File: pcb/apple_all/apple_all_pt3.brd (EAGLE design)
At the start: 56 x 65 mm, 49 parts, among them IC1 STM32F072C8T6, SW1 324_SW, SW2 324_SW, SW3 324_SW

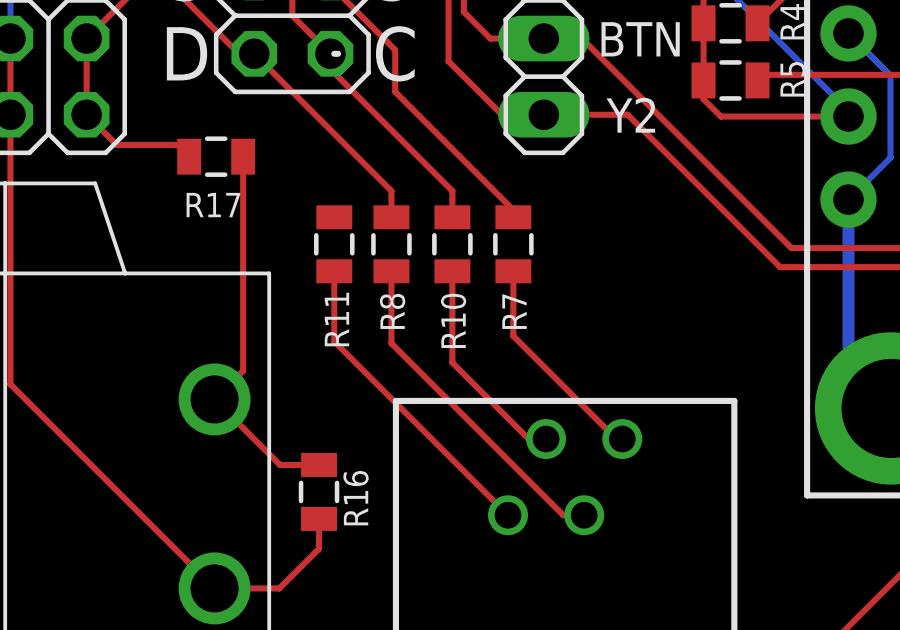
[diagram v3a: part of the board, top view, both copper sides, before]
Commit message: m0110 keyboard working, added busy signal and protocol switching
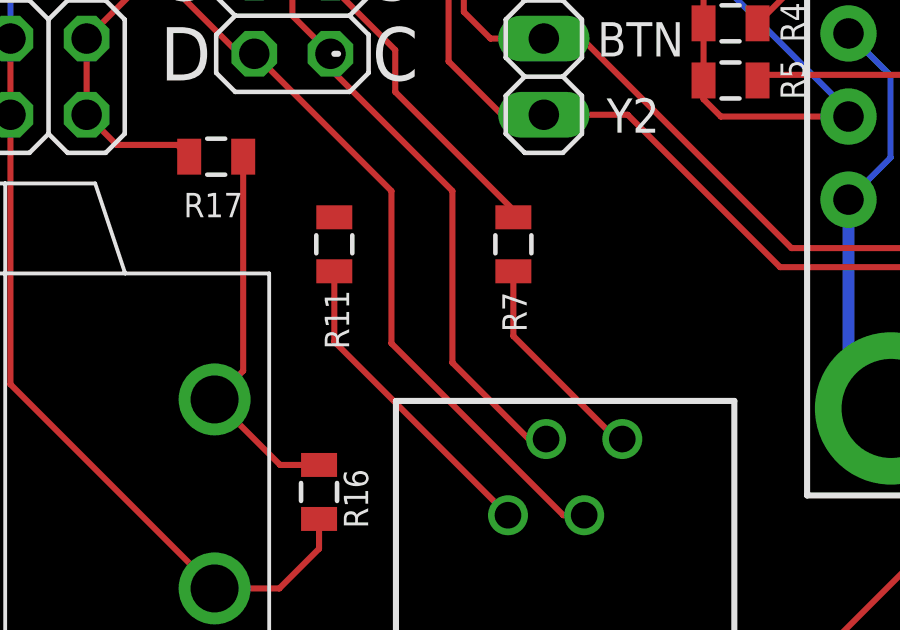
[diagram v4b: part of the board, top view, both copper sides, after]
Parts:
- removed R10, R8: 200, SparkFun-Passives:0805
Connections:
- removed net N$10: R8.2, U$8.3
- removed net N$20: R10.2, U$8.2
- net N$19: now also U$8.2; no longer R10.1
- net N$25: now also U$8.3; no longer R8.1
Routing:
- net N$25: track 14.9 -> 27.9 mm
- net N$10: track 11.2 -> 0.00 mm
- net N$19: track 16.5 -> 25.6 mm
- net N$20: track 7.22 -> 0.00 mm
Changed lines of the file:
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@@
 <layer number="19" name="Unrouted" color="6" fill="1" visible="yes" active="yes"/>
 <layer number="20" name="Dimension" color="24" fill="1" visible="yes" active="yes"/>
-<layer number="21" name="tPlace" color="7" fill="1" visible="yes" active="yes"/>
-<layer number="22" name="bPlace" color="7" fill="1" visible="yes" active="yes"/>
+<layer number="21" name="tPlace" color="7" fill="1" visible="no" active="yes"/>
+<layer number="22" name="bPlace" color="7" fill="1" visible="no" active="yes"/>
 <layer number="23" name="tOrigins" color="15" fill="1" visible="yes" active="yes"/>
 <layer number="24" name="bOrigins" color="15" fill="1" visible="yes" active="yes"/>
-<layer number="25" name="tNames" color="7" fill="1" visible="yes" active="yes"/>
-<layer number="26" name="bNames" color="7" fill="1" visible="yes" active="yes"/>
-<layer number="27" name="tValues" color="7" fill="1" visible="yes" active="yes"/>
-<layer number="28" name="bValues" color="7" fill="1" visible="yes" active="yes"/>
+<layer number="25" name="tNames" color="7" fill="1" visible="no" active="yes"/>
+<layer number="26" name="bNames" color="7" fill="1" visible="no" active="yes"/>
+<layer number="27" name="tValues" color="7" fill="1" visible="no" active="yes"/>
+<layer number="28" name="bValues" color="7" fill="1" visible="no" active="yes"/>
 <layer number="29" name="tStop" color="7" fill="3" visible="no" active="yes"/>
 <layer number="30" name="bStop" color="7" fill="6" visible="no" active="yes"/>
@@
 <layer number="49" name="Reference" color="7" fill="1" visible="no" active="yes"/>
 <layer number="50" name="dxf" color="7" fill="1" visible="no" active="no"/>
-<layer number="51" name="tDocu" color="7" fill="1" visible="yes" active="yes"/>
-<layer number="52" name="bDocu" color="7" fill="1" visible="yes" active="yes"/>
+<layer number="51" name="tDocu" color="7" fill="1" visible="no" active="yes"/>
+<layer number="52" name="bDocu" color="7" fill="1" visible="no" active="yes"/>
 <layer number="53" name="tGND_GNDA" color="7" fill="1" visible="no" active="no"/>
 <layer number="54" name="bGND_GNDA" color="7" fill="1" visible="no" active="no"/>
@@
 <attribute name="NAME" x="34.3535" y="19.05" size="0.8128" layer="25" rot="R90"/>
 </element>
-<element name="R8" library="SparkFun-Passives" package="0805" value="200" x="29.845" y="21.971" smashed="yes" rot="R270">
-<attribute name="NAME" x="30.2895" y="19.05" size="0.8128" layer="25" rot="R90"/>
-</element>
-<element name="R10" library="SparkFun-Passives" package="0805" value="200" x="31.877" y="21.971" smashed="yes" rot="R270">
-<attribute name="NAME" x="32.3215" y="18.415" size="0.8128" layer="25" rot="R90"/>
-</element>
 <element name="R11" library="SparkFun-Passives" package="0805" value="200" x="27.94" y="21.971" smashed="yes" rot="R270">
 <attribute name="NAME" x="27.6225" y="20.447" size="0.8128" layer="25" rot="R270"/>
@@
 <wire x1="37.54" y1="15.48" x2="37.341" y2="15.48" width="0.2032" layer="1"/>
 </signal>
-<signal name="N$10">
-<contactref element="U$8" pad="3"/>
-<contactref element="R8" pad="2"/>
-<wire x1="29.845" y1="21.071" x2="29.845" y2="18.669" width="0.2032" layer="1"/>
-<wire x1="35.574" y1="12.94" x2="36.27" y2="12.94" width="0.2032" layer="1"/>
-<wire x1="29.845" y1="18.669" x2="35.574" y2="12.94" width="0.2032" layer="1"/>
-</signal>
-<signal name="N$20">
-<contactref element="U$8" pad="2"/>
-<contactref element="R10" pad="2"/>
-<wire x1="34.42" y1="15.48" x2="31.877" y2="18.023" width="0.2032" layer="1"/>
-<wire x1="31.877" y1="21.071" x2="31.877" y2="18.023" width="0.2032" layer="1"/>
-<wire x1="34.42" y1="15.48" x2="35" y2="15.48" width="0.2032" layer="1"/>
-</signal>
 <signal name="N$21">
 <contactref element="U$8" pad="1"/>
@@
 <contactref element="JP3" pad="4"/>
 <contactref element="IC1" pad="21"/>
-<contactref element="R10" pad="1"/>
-<wire x1="27.813" y1="27.813" x2="31.877" y2="23.749" width="0.2032" layer="1"/>
 <wire x1="27.813" y1="28.321" x2="27.813" y2="27.813" width="0.2032" layer="1"/>
-<wire x1="31.877" y1="23.749" x2="31.877" y2="22.871" width="0.2032" layer="1"/>
 <wire x1="27.813" y1="28.321" x2="26.543" y2="29.591" width="0.2032" layer="1"/>
 <wire x1="26.543" y1="31.75" x2="26.035" y2="32.258" width="0.2032" layer="1"/>
@@
 <wire x1="26.543" y1="29.591" x2="26.543" y2="31.75" width="0.2032" layer="1"/>
 <wire x1="23.749" y1="32.258" x2="23.25" y2="32.757" width="0.2032" layer="1"/>
+<contactref element="U$8" pad="2"/>
+<wire x1="31.877" y1="18.023" x2="34.42" y2="15.48" width="0.2032" layer="1"/>
+<wire x1="34.42" y1="15.48" x2="35" y2="15.48" width="0.2032" layer="1"/>
+<wire x1="27.813" y1="27.813" x2="31.877" y2="23.749" width="0.2032" layer="1"/>
+<wire x1="31.877" y1="23.749" x2="31.877" y2="18.023" width="0.2032" layer="1"/>
 </signal>
 <signal name="N$25">
-<contactref element="R8" pad="1"/>
 <contactref element="JP3" pad="3"/>
 <contactref element="IC1" pad="20"/>
-<wire x1="25.273" y1="28.321" x2="29.845" y2="23.749" width="0.2032" layer="1"/>
-<wire x1="29.845" y1="23.749" x2="29.845" y2="22.871" width="0.2032" layer="1"/>
 <wire x1="22.75" y1="34.5" x2="22.75" y2="30.336" width="0.2032" layer="1"/>
 <wire x1="24.765" y1="28.321" x2="25.273" y2="28.321" width="0.2032" layer="1"/>
 <wire x1="22.75" y1="30.336" x2="24.765" y2="28.321" width="0.2032" layer="1"/>
+<contactref element="U$8" pad="3"/>
+<wire x1="35.574" y1="12.94" x2="36.27" y2="12.94" width="0.2032" layer="1"/>
+<wire x1="29.845" y1="18.669" x2="35.574" y2="12.94" width="0.2032" layer="1"/>
+<wire x1="25.273" y1="28.321" x2="29.845" y2="23.749" width="0.2032" layer="1"/>
+<wire x1="29.845" y1="23.749" x2="29.845" y2="18.669" width="0.2032" layer="1"/>
 </signal>
 <signal name="N$31">
